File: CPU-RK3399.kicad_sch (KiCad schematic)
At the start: 0 parts

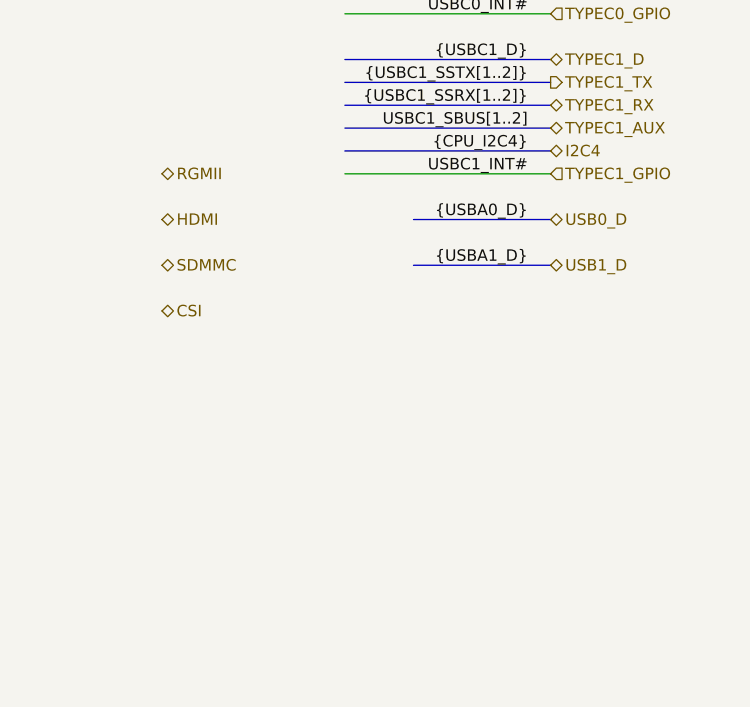
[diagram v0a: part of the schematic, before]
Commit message: update schematic
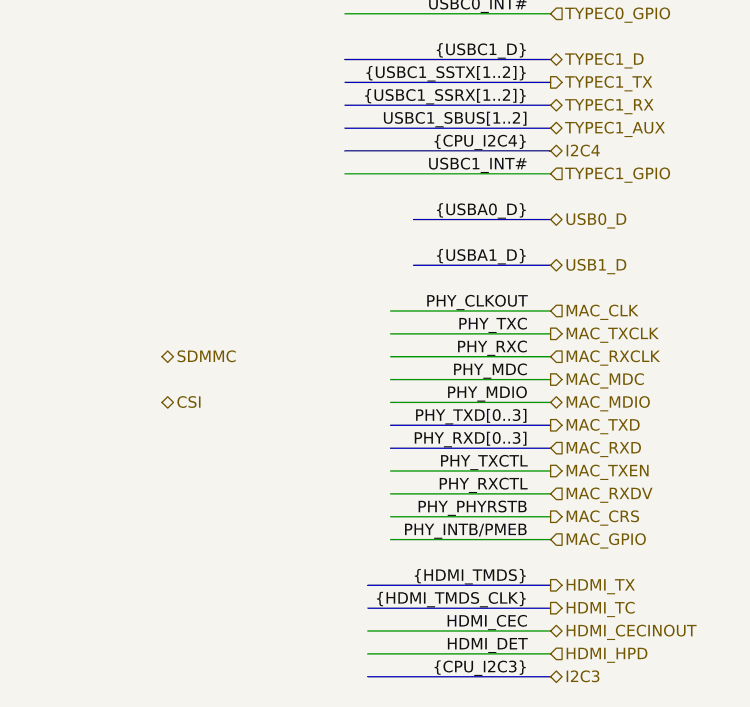
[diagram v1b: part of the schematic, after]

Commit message: update root schematic
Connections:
- no-connect marks 0 -> 33

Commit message: design CPU Power
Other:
- added sheet CPU-RK3399 PMU Controller (CPU-RK3399_PMU_Controller.kicad_sch)
- added sheet CPU-RK3399 Power (CPU-RK3399_Power.kicad_sch)
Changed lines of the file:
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@@
 	(generator "eeschema")
 	(generator_version "9.0")
-	(paper "A4")
+	(paper "A3")
 	(title_block
 		(title "CPU-RK3399")
@@
 		)
 	)
+	(wire
+		(pts
+			(xy 314.96 53.34) (xy 317.5 53.34)
+		)
+		(stroke
+			(width 0)
+			(type default)
+		)
+	)
 	(bus
 		(pts
@@
 		)
 	)
+	(wire
+		(pts
+			(xy 314.96 50.8) (xy 317.5 50.8)
+		)
+		(stroke
+			(width 0)
+			(type default)
+		)
+	)
 	(bus
 		(pts
@@
 		)
 	)
+	(hierarchical_label "VDD_CPU_B_FB"
+		(shape output)
+		(at 314.96 50.8 180)
+		(effects
+			(font
+				(size 1.27 1.27)
+			)
+			(justify right)
+		)
+	)
 	(hierarchical_label "EMMC_DATA"
 		(shape bidirectional)
@@
 		)
 	)
+	(hierarchical_label "VDD_GPU_FB"
+		(shape output)
+		(at 314.96 53.34 180)
+		(effects
+			(font
+				(size 1.27 1.27)
+			)
+			(justify right)
+		)
+	)
 	(hierarchical_label "MIPI_RX0_D"
 		(shape input)
@@
 		)
 	)
+	(sheet
+		(at 317.5 48.26)
+		(size 17.78 7.62)
+		(exclude_from_sim no)
+		(in_bom yes)
+		(on_board yes)
+		(dnp no)
+		(fields_autoplaced yes)
+		(stroke
+			(width 0.1524)
+			(type solid)
+		)
+		(fill
+			(color 0 0 0 0.0000)
+		)
+		(property "Sheetname" "CPU-RK3399 Power"
+			(at 317.5 47.5484 0)
+			(effects
+				(font
+					(size 1.27 1.27)
+				)
+				(justify left bottom)
+			)
+		)
+		(property "Sheetfile" "CPU-RK3399_Power.kicad_sch"
+			(at 317.5 56.4646 0)
+			(effects
+				(font
+					(size 1.27 1.27)
+				)
+				(justify left top)
+			)
+		)
+		(pin "VDD_CPU_B_FB" output
+			(at 317.5 50.8 180)
+			(effects
+				(font
+					(size 1.27 1.27)
+				)
+				(justify left)
+			)
+		)
+		(pin "VDD_GPU_FB" output
+			(at 317.5 53.34 180)
+			(effects
+				(font
+					(size 1.27 1.27)
+				)
+				(justify left)
+			)
+		)
+		(instances
+			(project "VESA-SBC3399"
+				(path "/ebc9dc57-8b05-484a-a5cd-c53b1efc71d3/a7299b18-4123-434b-8c69-0b9524fffa12"
+					(page "19")
+				)
+			)
+		)
+	)
+	(sheet
+		(at 317.5 63.5)
+		(size 17.78 5.08)
+		(exclude_from_sim no)
+		(in_bom yes)
+		(on_board yes)
+		(dnp no)
+		(fields_autoplaced yes)
+		(stroke
+			(width 0.1524)
+			(type solid)
+		)
+		(fill
+			(color 0 0 0 0.0000)
+		)
+		(property "Sheetname" "CPU-RK3399 PMU Controller"
+			(at 317.5 62.7884 0)
+			(effects
+				(font
+					(size 1.27 1.27)
+				)
+				(justify left bottom)
+			)
+		)
+		(property "Sheetfile" "CPU-RK3399_PMU_Controller.kicad_sch"
+			(at 317.5 69.1646 0)
+			(effects
+				(font
+					(size 1.27 1.27)
+				)
+				(justify left top)
+			)
+		)
+		(instances
+			(project "VESA-SBC3399"
+				(path "/ebc9dc57-8b05-484a-a5cd-c53b1efc71d3/a7299b18-4123-434b-8c69-0b9524fffa12"
+					(page "20")
+				)
+			)
+		)
+	)

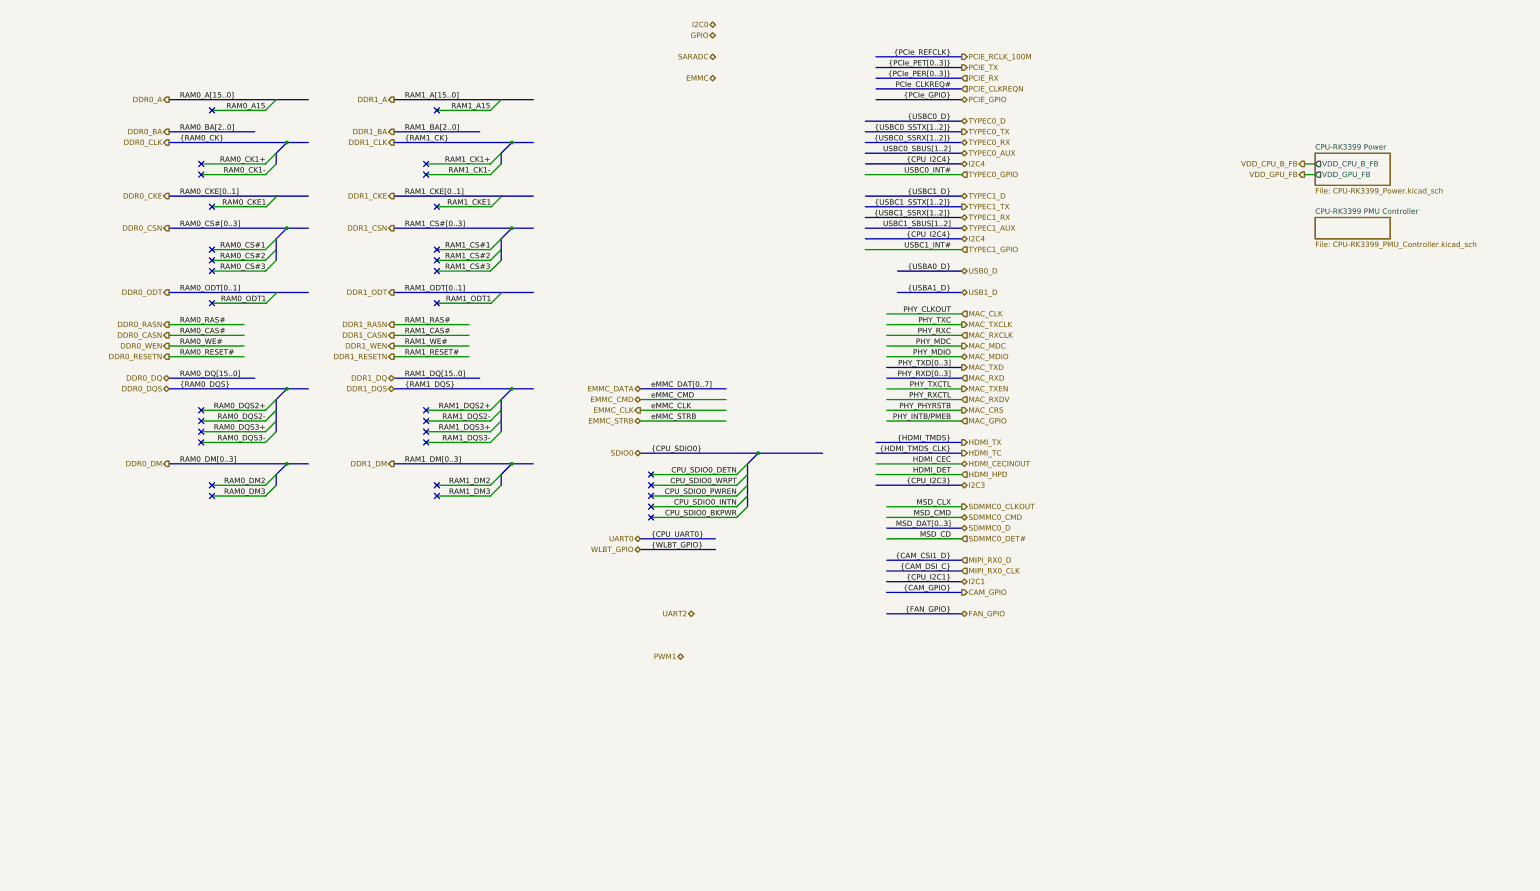
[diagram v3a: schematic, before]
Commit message: design CPU DDR
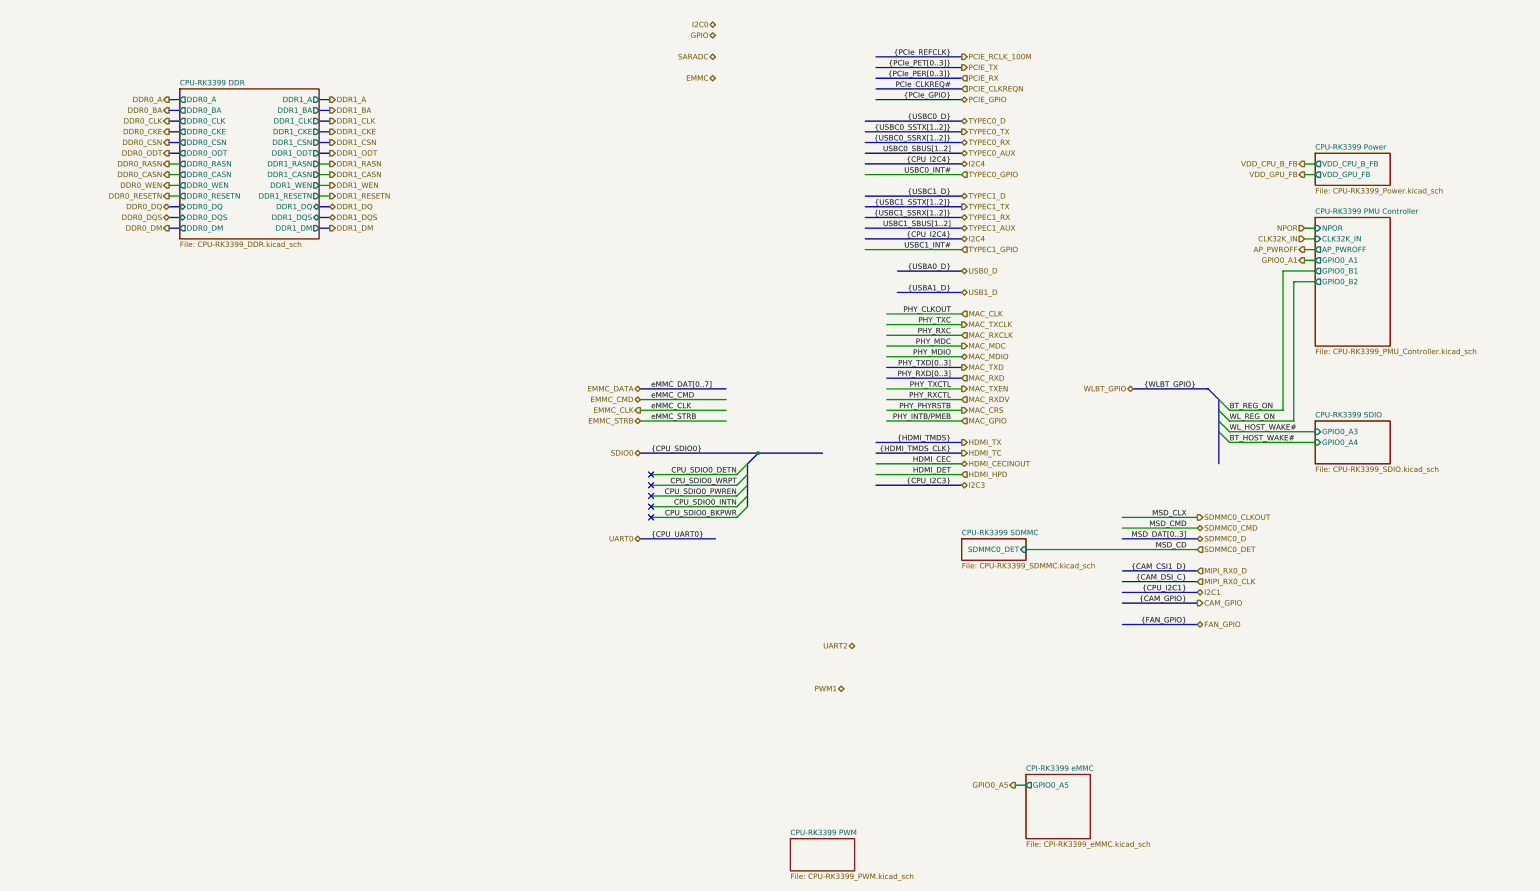
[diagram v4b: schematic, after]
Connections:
- no-connect marks 33 -> 5
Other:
- added sheet CPI-RK3399 eMMC (CPI-RK3399_eMMC.kicad_sch)
- added sheet CPU-RK3399 DDR (CPU-RK3399_DDR.kicad_sch)
- added sheet CPU-RK3399 PWM (CPU-RK3399_PWM.kicad_sch)
- added sheet CPU-RK3399 SDIO (CPU-RK3399_SDIO.kicad_sch)
- added sheet CPU-RK3399 SDMMC (CPU-RK3399_SDMMC.kicad_sch)
- sheet CPU-RK3399 PMU Controller ports: added AP_PWROFF, CLK32K_IN, GPIO0_A1, GPIO0_B1, GPIO0_B2, NPOR; removed none

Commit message: design CPU-RK3399 eMMC Controller
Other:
- sheet CPI-RK3399 eMMC renamed CPU-RK3399 eMMC
- sheet CPU-RK3399 eMMC: file CPI-RK3399_eMMC.kicad_sch -> CPU-RK3399_eMMC.kicad_sch
- company: (none) -> TickLab
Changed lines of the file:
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@@
 	(title_block
 		(title "CPU-RK3399")
-		(date "2026-01-09")
+		(date "2026-01-14")
 		(rev "1.0.0")
+		(company "TickLab")
 	)
 	(bus_alias "CAM_GPIO"
@@
 			(color 0 0 0 0.0000)
 		)
-		(property "Sheetname" "CPI-RK3399 eMMC"
+		(property "Sheetname" "CPU-RK3399 eMMC"
 			(at 248.92 194.8684 0)
 			(effects
@@
 			)
 		)
-		(property "Sheetfile" "CPI-RK3399_eMMC.kicad_sch"
+		(property "Sheetfile" "CPU-RK3399_eMMC.kicad_sch"
 			(at 248.92 211.4046 0)
 			(effects

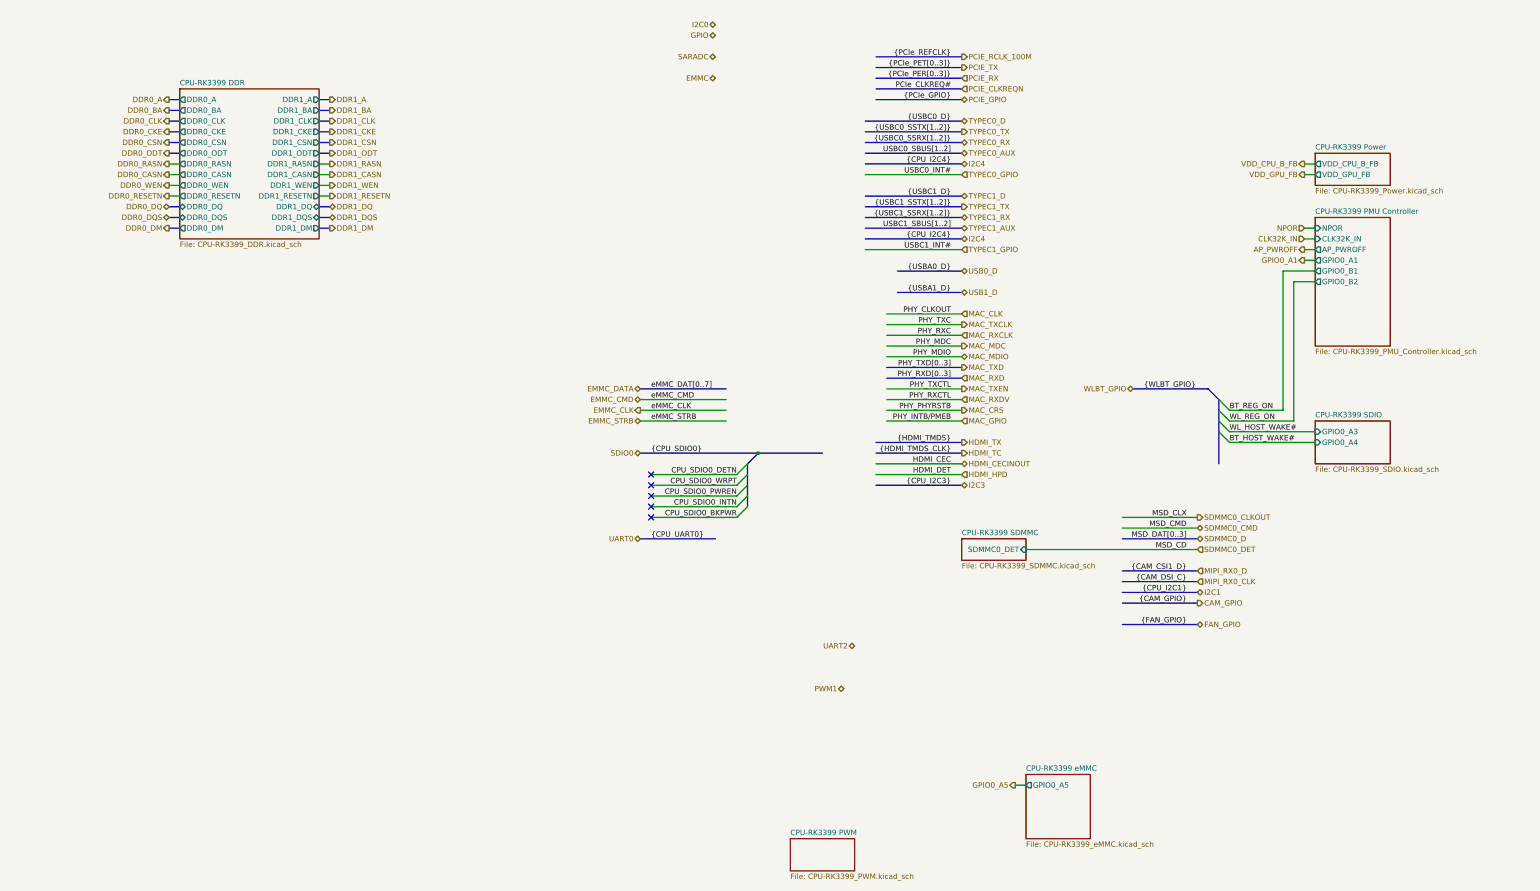
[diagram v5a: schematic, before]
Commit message: design CPU-RK3399 SDMMC
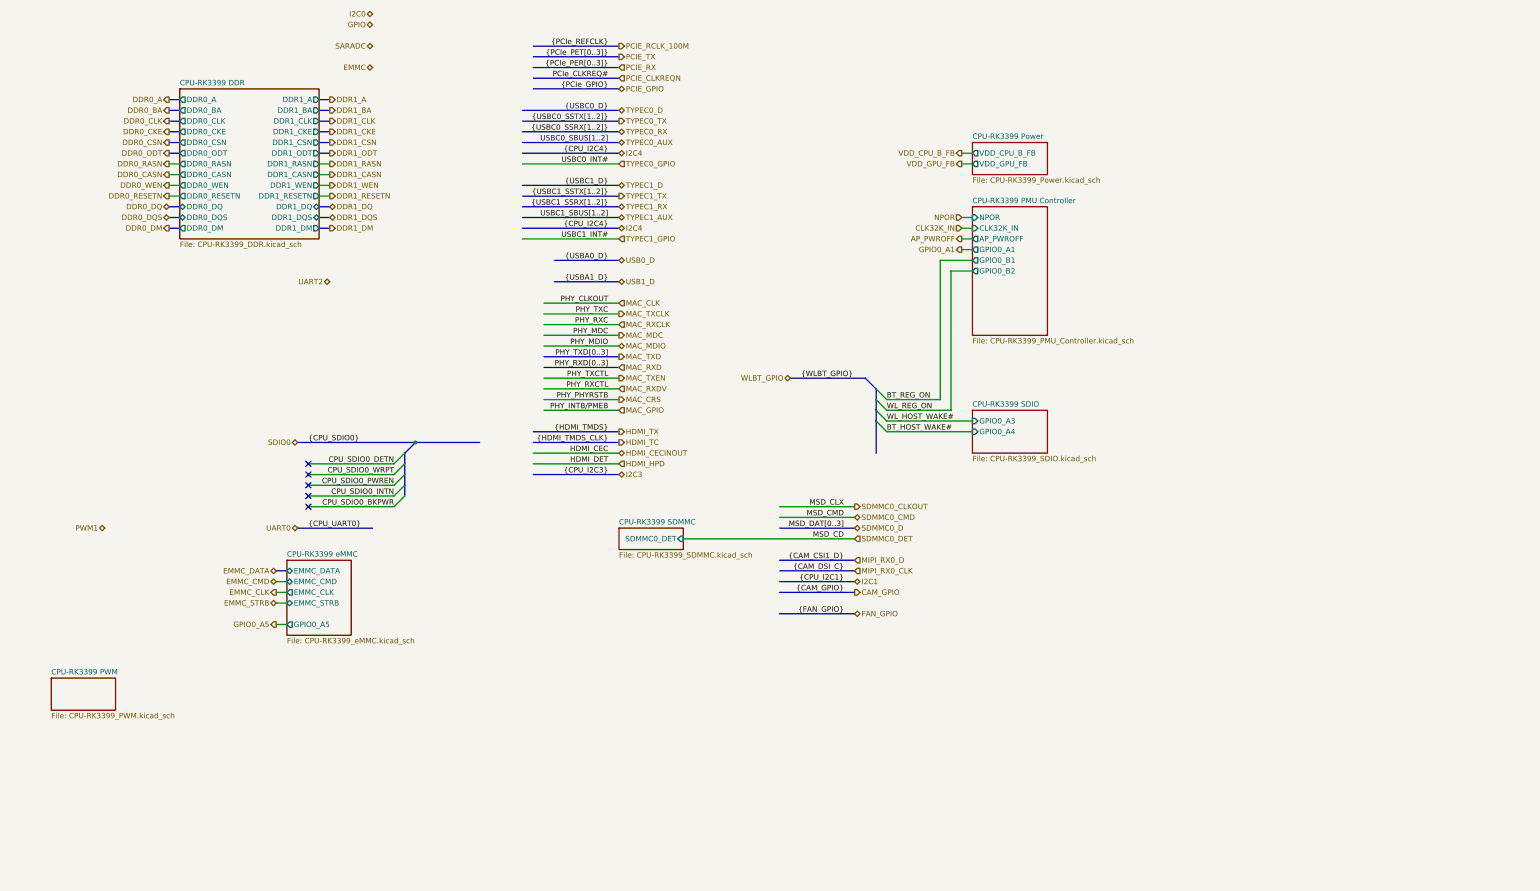
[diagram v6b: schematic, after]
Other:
- sheet CPU-RK3399 eMMC ports: added EMMC_CLK, EMMC_CMD, EMMC_DATA, EMMC_STRB; removed none
